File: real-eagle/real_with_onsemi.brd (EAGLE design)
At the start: 104.1 x 123.4 mm, 49 parts, among them J2 POWER_JACK

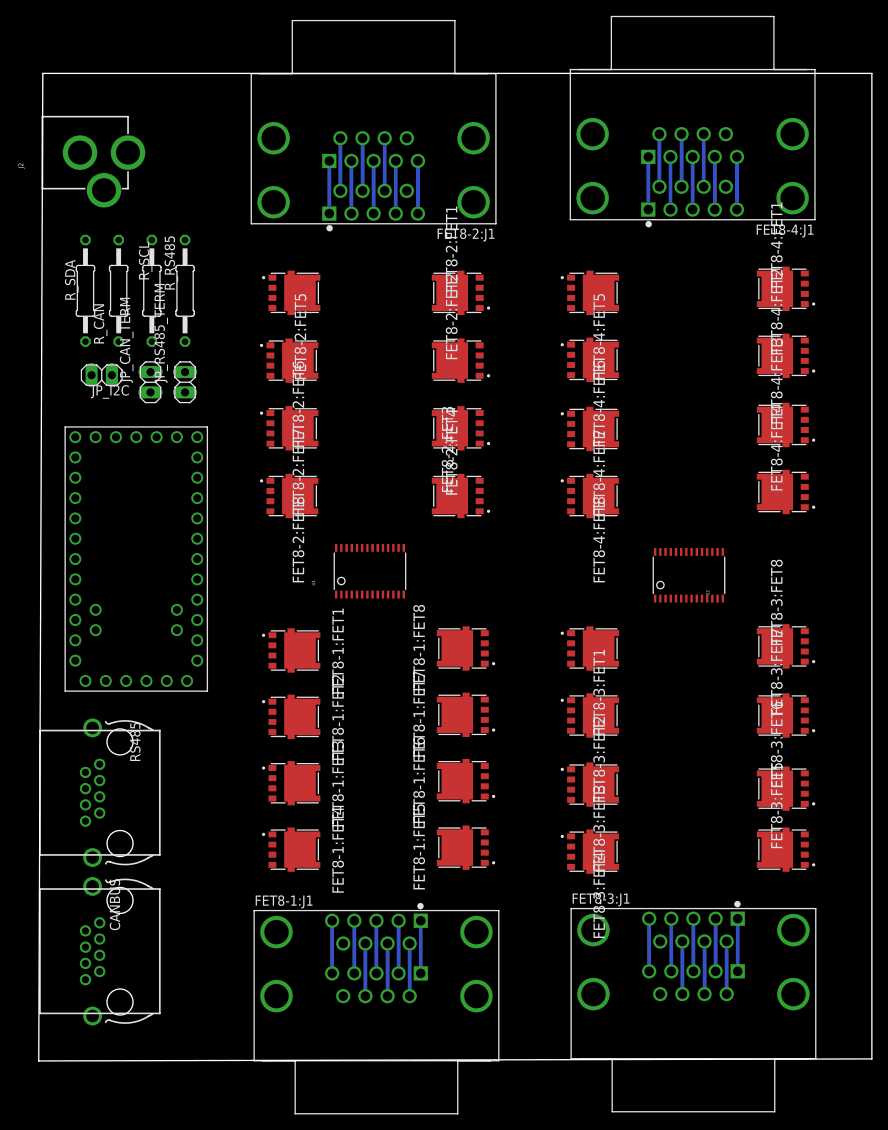
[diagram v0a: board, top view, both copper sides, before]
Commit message: Routed except vcc/gnd
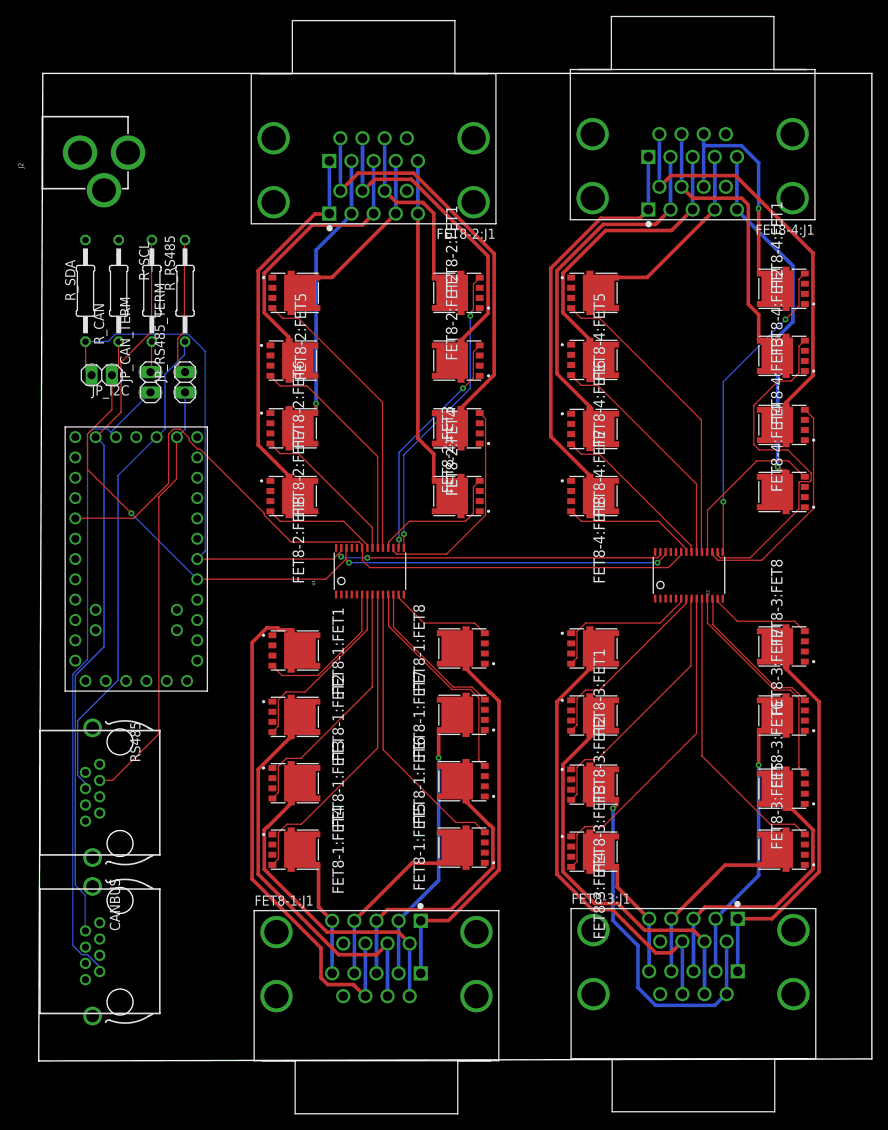
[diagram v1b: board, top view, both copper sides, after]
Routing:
- net N$19: track 0.00 -> 106.9 mm, vias 0 -> 2
- net N$16: track 0.00 -> 99.0 mm, vias 0 -> 3
- net ENABLE: track 0.00 -> 93.6 mm
- net N$4: track 0.00 -> 91.8 mm
- net N$3: track 0.00 -> 81.0 mm
- net N$5: track 0.00 -> 61.9 mm
- net HEATER_A0: track 6.58 -> 64.3 mm
- net N$7: track 0.00 -> 53.9 mm
- net HEATER_C0: track 6.58 -> 54.3 mm
- net HEATER_B2: track 6.58 -> 51.9 mm
- net PWM_D1: track 0.00 -> 44.3 mm
- net HEATER_D2: track 6.58 -> 50.7 mm
- net HEATER_D7: track 6.58 -> 49.8 mm
- net PWM_C3: track 0.00 -> 41.4 mm
- net PWM_A3: track 0.00 -> 40.3 mm
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
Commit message: Rename FET8-X->FX, move names/values for silkscreen
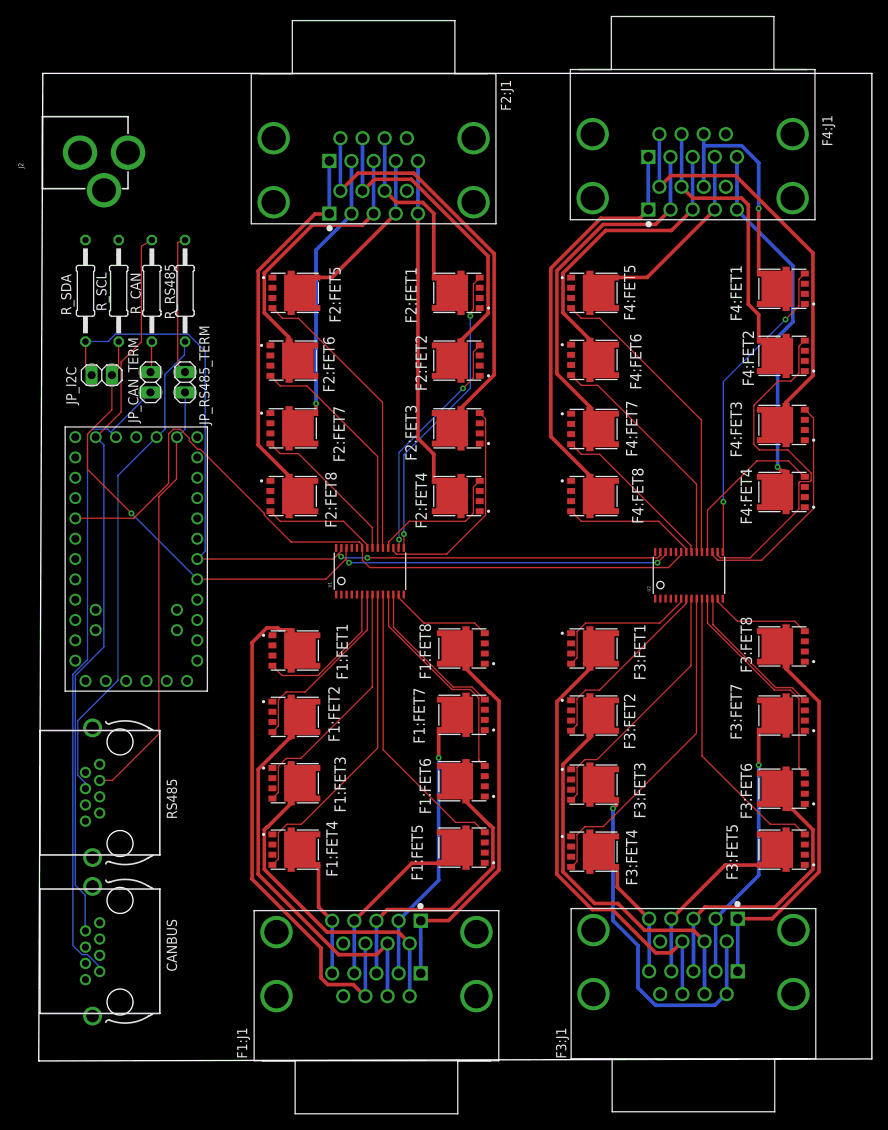
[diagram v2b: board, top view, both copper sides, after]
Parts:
- renumbered FET8-1:FET1 to F1:FET1, FET8-1:FET2 to F1:FET2, FET8-1:FET3 to F1:FET3, FET8-1:FET4 to F1:FET4, FET8-1:FET5 to F1:FET5, FET8-1:FET6 to F1:FET6, FET8-1:FET7 to F1:FET7, FET8-1:FET8 to F1:FET8, FET8-1:J1 to F1:J1, FET8-2:FET1 to F2:FET1, FET8-2:FET2 to F2:FET2, FET8-2:FET3 to F2:FET3, FET8-2:FET4 to F2:FET4, FET8-2:FET5 to F2:FET5, FET8-2:FET6 to F2:FET6, FET8-2:FET7 to F2:FET7, FET8-2:FET8 to F2:FET8, FET8-2:J1 to F2:J1, FET8-3:FET1 to F3:FET1, FET8-3:FET2 to F3:FET2, FET8-3:FET3 to F3:FET3, FET8-3:FET4 to F3:FET4, FET8-3:FET5 to F3:FET5, FET8-3:FET6 to F3:FET6, FET8-3:FET7 to F3:FET7, FET8-3:FET8 to F3:FET8, FET8-3:J1 to F3:J1, FET8-4:FET1 to F4:FET1, FET8-4:FET2 to F4:FET2, FET8-4:FET3 to F4:FET3, FET8-4:FET4 to F4:FET4, FET8-4:FET5 to F4:FET5, FET8-4:FET6 to F4:FET6, FET8-4:FET7 to F4:FET7, FET8-4:FET8 to F4:FET8, FET8-4:J1 to F4:J1
